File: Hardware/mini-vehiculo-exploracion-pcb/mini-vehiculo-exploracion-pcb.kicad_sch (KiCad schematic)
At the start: 23 parts, among them IC1 BME690, J1 ArducamMINIOV2640, J3 Drivers_Conn_1x8, J4 Drivers_Conn_1x4, J5 Aux_Conn_1x4, J6 RC_Conn_1x4, U1 BNO086, U2 ESP32-S3-WROOM-1, Y1 830003000

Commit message: Add battery sensor
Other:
- sheet MCU renamed MCU_Peripherals
- added sheet Battery_sensor (battery_sensor.kicad_sch)
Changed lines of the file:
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@@
 	)
 	(sheet
-		(at 234.95 90.17)
-		(size 40.64 24.13)
+		(at 234.315 138.43)
+		(size 33.02 17.145)
 		(exclude_from_sim no)
 		(in_bom yes)
@@
 			(color 0 0 0 0.0000)
 		)
-		(property "Sheetname" "MCU"
+		(property "Sheetname" "Battery_sensor"
+			(at 234.315 137.7184 0)
+			(effects
+				(font
+					(size 1.27 1.27)
+				)
+				(justify left bottom)
+			)
+		)
+		(property "Sheetfile" "battery_sensor.kicad_sch"
+			(at 234.315 156.1596 0)
+			(effects
+				(font
+					(size 1.27 1.27)
+				)
+				(justify left top)
+			)
+		)
+		(instances
+			(project "mini-vehiculo-exploracion-pcb"
+				(path "/3cb3b833-c38f-47b4-b7e9-f0e6337b7613"
+					(page "4")
+				)
+			)
+		)
+	)
+	(sheet
+		(at 234.95 90.17)
+		(size 32.385 17.145)
+		(exclude_from_sim no)
+		(in_bom yes)
+		(on_board yes)
+		(dnp no)
+		(fields_autoplaced yes)
+		(stroke
+			(width 0.1524)
+			(type solid)
+		)
+		(fill
+			(color 0 0 0 0.0000)
+		)
+		(property "Sheetname" "MCU_Peripherals"
 			(at 234.95 89.4584 0)
 			(effects
@@
 		)
 		(property "Sheetfile" "mcu.kicad_sch"
-			(at 234.95 114.8846 0)
+			(at 234.95 107.8996 0)
 			(effects
 				(font
@@
 	)
 	(sheet
-		(at 234.95 124.46)
+		(at 234.315 114.3)
 		(size 33.02 16.51)
 		(exclude_from_sim no)
@@
 		)
 		(property "Sheetname" "Electrical"
-			(at 234.95 123.7484 0)
+			(at 234.315 113.5884 0)
 			(effects
 				(font
@@
 		)
 		(property "Sheetfile" "electrical.kicad_sch"
-			(at 234.95 141.5546 0)
+			(at 234.315 131.3946 0)
 			(effects
 				(font

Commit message: changes
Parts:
- C1: footprint (none) -> Capacitor_SMD:C_0805_2012Metric_Pad1.18x1.45mm_HandSolder
- IC1: footprint BME690 -> BME690:BME690
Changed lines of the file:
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@@
 			)
 		)
-		(property "Footprint" "BME690"
+		(property "Footprint" "BME690:BME690"
 			(at 139.7 204.14 0)
 			(effects
@@
 			)
 		)
-		(property "Footprint" ""
+		(property "Footprint" "Capacitor_SMD:C_0805_2012Metric_Pad1.18x1.45mm_HandSolder"
 			(at 35.2552 44.45 0)
 			(effects

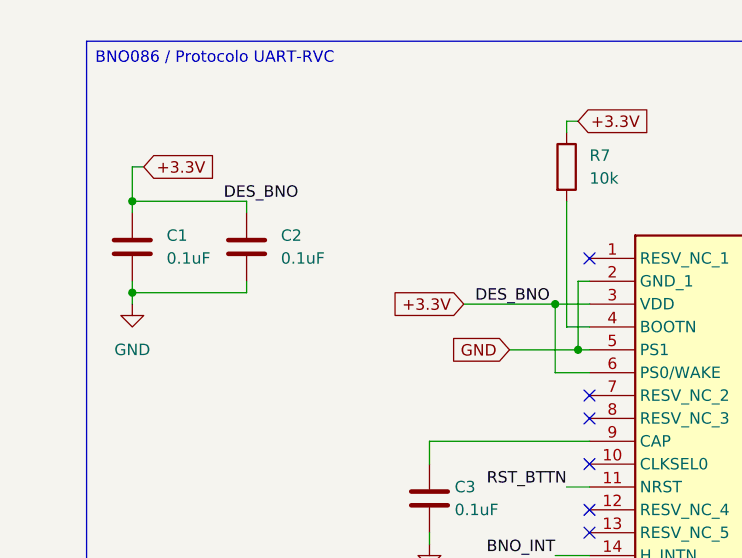
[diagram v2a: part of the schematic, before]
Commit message: Add footprints
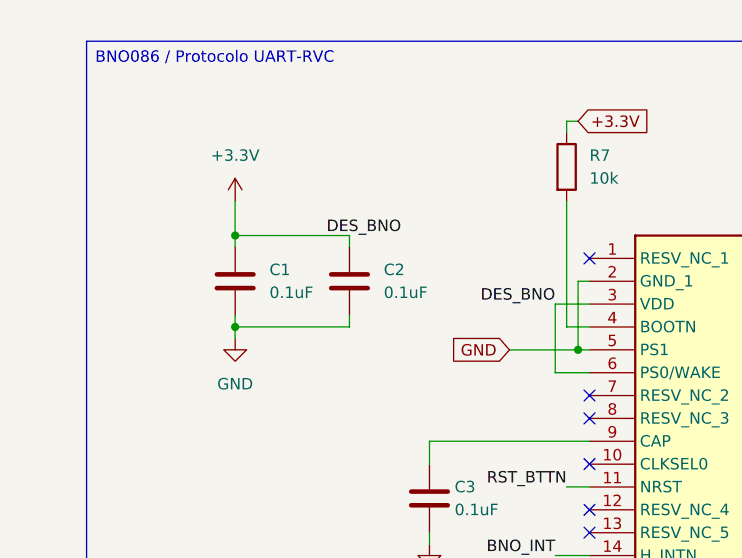
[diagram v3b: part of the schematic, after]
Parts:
- C2, C3, C4, C5, C6, C7: footprint (none) -> Capacitor_SMD:C_0805_2012Metric_Pad1.18x1.45mm_HandSolder
- J3: footprint (none) -> Connector_PinSocket_2.54mm:PinSocket_1x08_P2.54mm_Vertical
- J4, J5, J6: footprint (none) -> Connector_PinSocket_2.54mm:PinSocket_1x04_P2.54mm_Vertical
- R1, R2, R5, R6, R7, R8, R9: footprint (none) -> Resistor_SMD:R_0805_2012Metric_Pad1.20x1.40mm_HandSolder
- U1: footprint BNO086 -> BNO086:BNO086
- Y1: footprint 830003000 -> 830003000:830003000
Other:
- moved on the sheet: C1, C2

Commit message: innit pcb
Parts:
- added J7: Battery_Terminal_01x02, TerminalBlock:TerminalBlock_Xinya_XY308-2.54-2P_1x02_P2.54mm_Horizontal, symbol Connector:Screw_Terminal_01x02
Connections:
- net GND: now also J7.2 (Pin_2)
- new net ENT_BAT: J7.1 (Pin_1)
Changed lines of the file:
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@@
 	(wire
 		(pts
+			(xy 140.97 160.02) (xy 149.86 160.02)
+		)
+		(stroke
+			(width 0)
+			(type default)
+		)
+	)
+	(wire
+		(pts
 			(xy 81.28 74.93) (xy 85.09 74.93)
 		)
@@
 	(wire
 		(pts
+			(xy 144.78 157.48) (xy 149.86 157.48)
+		)
+		(stroke
+			(width 0)
+			(type default)
+		)
+	)
+	(wire
+		(pts
 			(xy 146.05 109.22) (xy 146.05 96.52)
 		)
@@
 		)
 	)
+	(global_label "ENT_BAT"
+		(shape input)
+		(at 144.78 157.48 180)
+		(fields_autoplaced yes)
+		(effects
+			(font
+				(size 1.27 1.27)
+			)
+			(justify right)
+		)
+		(property "Intersheetrefs" "${INTERSHEET_REFS}"
+			(at 134.0539 157.48 0)
+			(effects
+				(font
+					(size 1.27 1.27)
+				)
+				(justify right)
+				(hide yes)
+			)
+		)
+	)
 	(global_label "+3.3V"
 		(shape input)
@@
 	(global_label "GND"
 		(shape input)
+		(at 140.97 160.02 180)
+		(fields_autoplaced yes)
+		(effects
+			(font
+				(size 1.27 1.27)
+			)
+			(justify right)
+		)
+		(property "Intersheetrefs" "${INTERSHEET_REFS}"
+			(at 134.1143 160.02 0)
+			(effects
+				(font
+					(size 1.27 1.27)
+				)
+				(justify right)
+				(hide yes)
+			)
+		)
+	)
+	(global_label "GND"
+		(shape input)
 		(at 137.16 67.31 0)
 		(fields_autoplaced yes)
@@
 					(unit 1)
 				)
+			)
+		)
+	)
+	(symbol
+		(lib_id "Connector:Screw_Terminal_01x02")
+		(at 154.94 157.48 0)
+		(unit 1)
+		(exclude_from_sim no)
+		(in_bom yes)
+		(on_board yes)
+		(dnp no)
+		(fields_autoplaced yes)
+		(property "Reference" "J7"
+			(at 157.48 157.4799 0)
+			(effects
+				(font
+					(size 1.27 1.27)
+				)
+				(justify left)
+			)
+		)
+		(property "Value" "Battery_Terminal_01x02"
+			(at 157.48 160.0199 0)
+			(effects
+				(font
+					(size 1.27 1.27)
+				)
+				(justify left)
+			)
+		)
+		(property "Footprint" "TerminalBlock:TerminalBlock_Xinya_XY308-2.54-2P_1x02_P2.54mm_Horizontal"
+			(at 154.94 157.48 0)
+			(effects
+				(font
+					(size 1.27 1.27)
+				)
+				(hide yes)
+			)
+		)
+		(property "Datasheet" "~"
+			(at 154.94 157.48 0)
+			(effects
+				(font
+					(size 1.27 1.27)
+				)
+				(hide yes)
+			)
+		)
+		(property "Description" "Generic screw terminal, single row, 01x02, script generated (kicad-library-utils/schlib/autogen/connector/)"
+			(at 154.94 157.48 0)
+			(effects
+				(font
+					(size 1.27 1.27)
+				)
+				(hide yes)
+			)
+		)
+		(pin "1"
+		)
+		(pin "2"
+		)
+		(instances
+			(project ""
+				(path "/3cb3b833-c38f-47b4-b7e9-f0e6337b7613"
+					(reference "J7")
+					(unit 1)
+				)

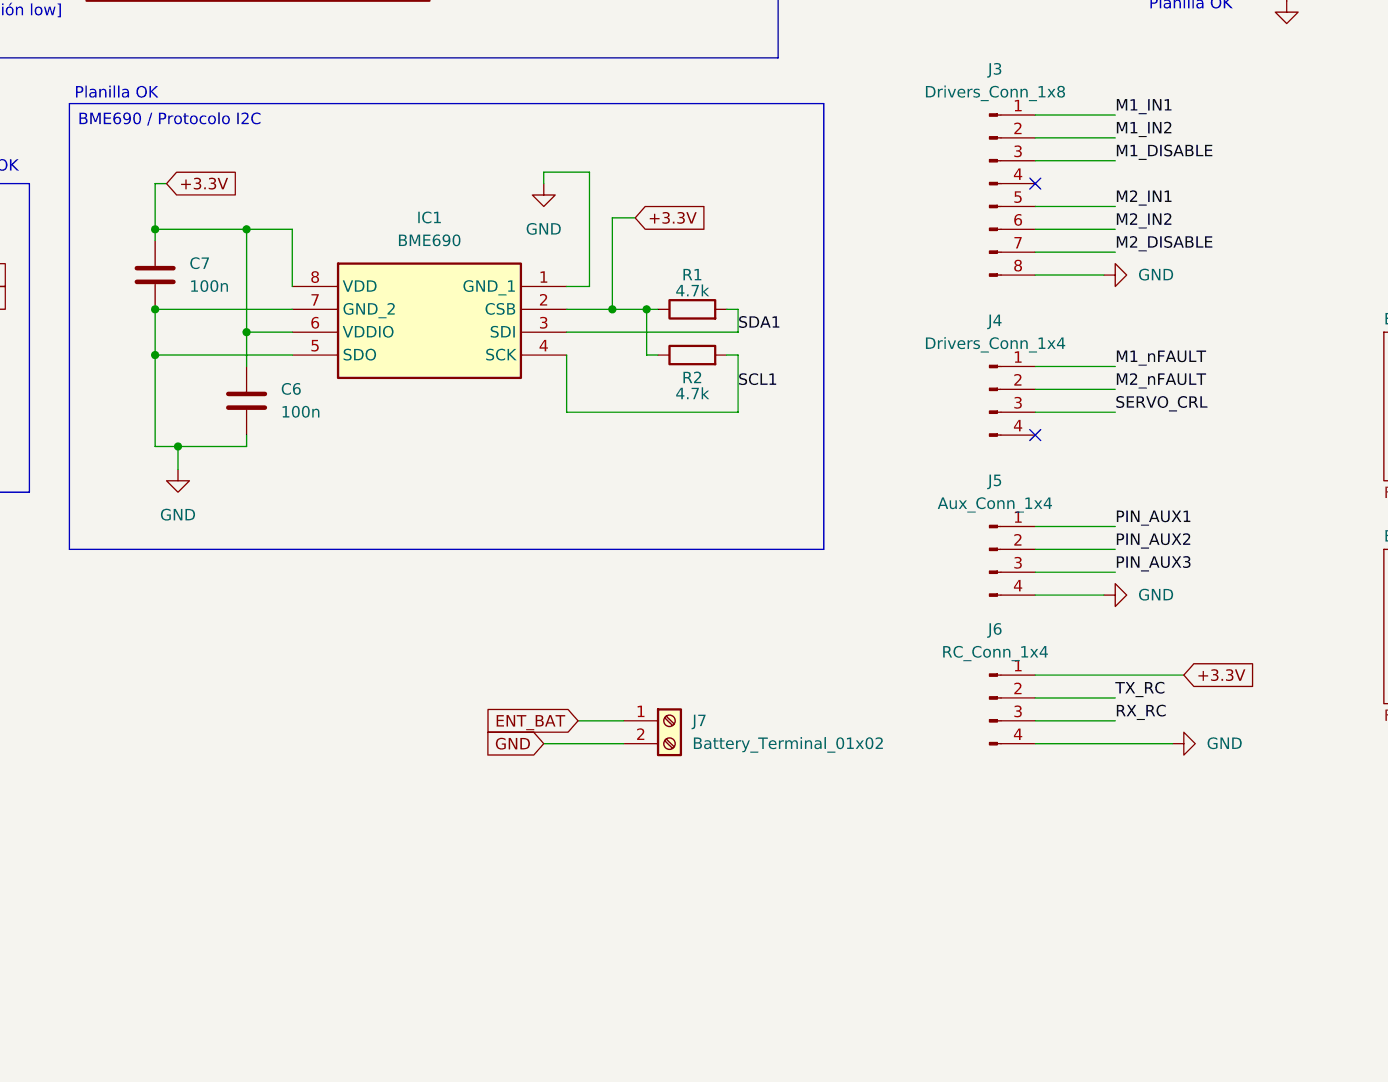
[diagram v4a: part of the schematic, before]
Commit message: Revert "fix bug pcb"
This reverts commit 95896929b2c40d1d86d6f174368d0f9d923b36b5.
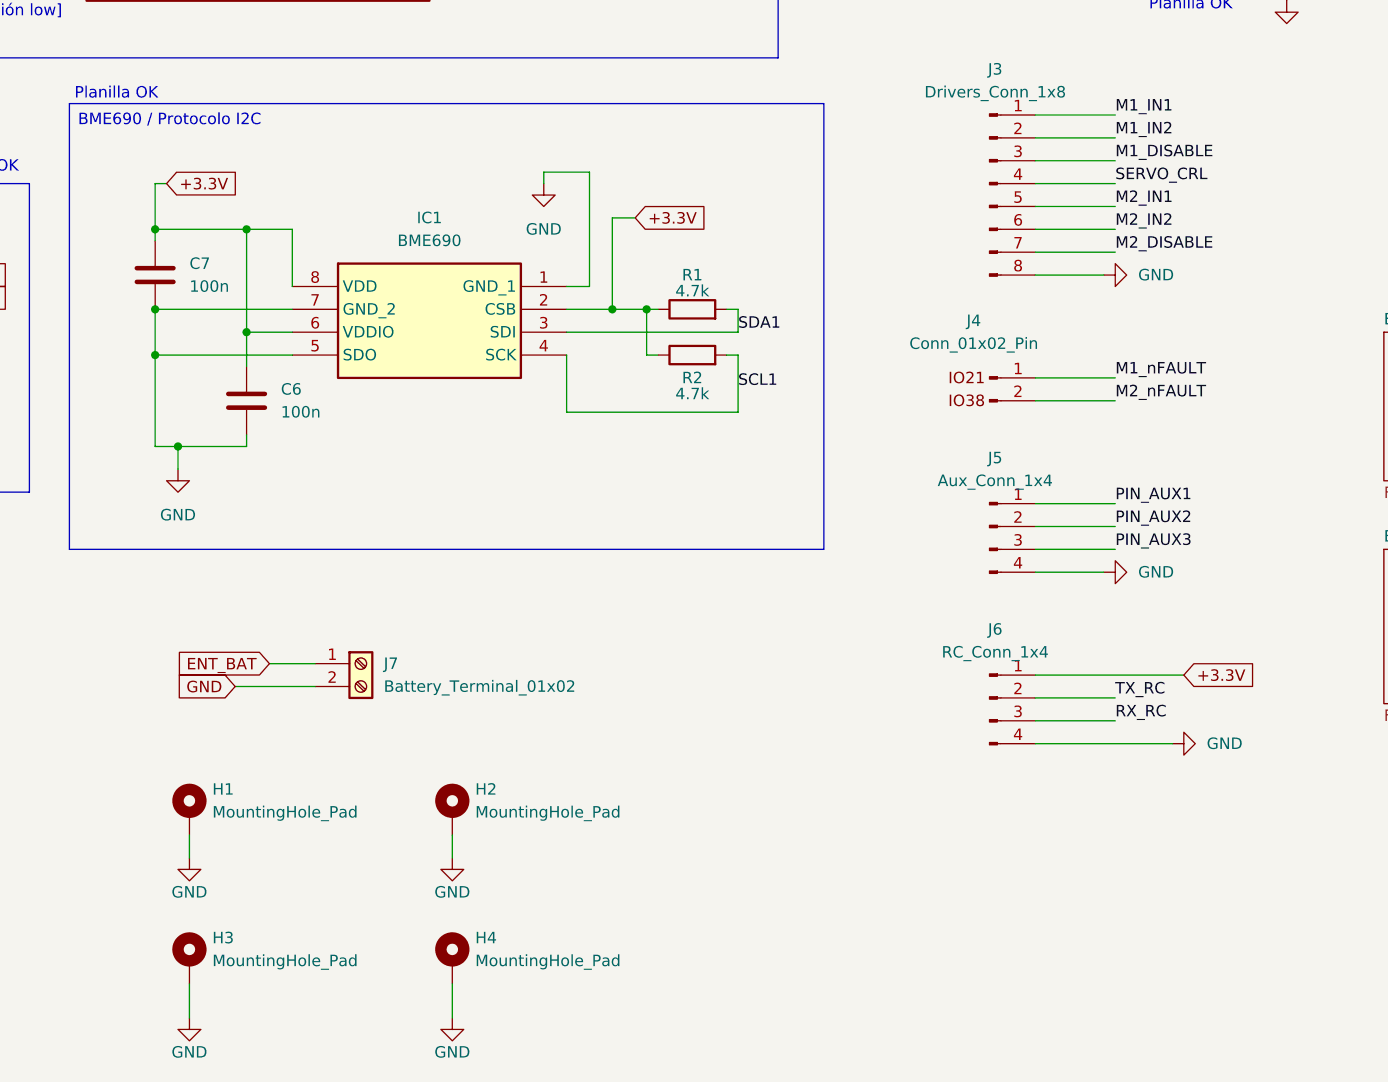
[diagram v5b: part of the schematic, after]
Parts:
- removed J4: Drivers_Conn_1x4, Connector_PinSocket_2.54mm:PinSocket_1x04_P2.54mm_Vertical, symbol Connector:Conn_01x04_Pin
- added H1, H2, H3, H4: MountingHole_Pad, MountingHole:MountingHole_3.2mm_M3_Pad_Via, symbol Mechanical:MountingHole_Pad
- added J4: Conn_01x02_Pin, Connector_PinSocket_2.54mm:PinSocket_1x02_P2.54mm_Vertical, symbol ConectorDriverESP:Conn_01x02_Pin
- J7: footprint TerminalBlock:TerminalBlock_Xinya_XY308-2.54-2P_1x02_P2.54mm_Horizontal -> TerminalBlock_Phoenix:TerminalBlock_Phoenix_MPT-0,5-2-2.54_1x02_P2.54mm_Horizontal
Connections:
- net GND: now also H1.1, H2.1, H3.1, H4.1
- net M1_nFAULT: now also J4.1 (Pin_1)
- net M2_nFAULT: now also J4.2 (Pin_2)
- net SERVO_CRL: now also J3.4 (Pin_4)
- no-connect marks 20 -> 18
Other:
- moved on the sheet: J5, J7

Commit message: continue pcb
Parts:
- added C23, C24: 0.1uF, Capacitor_SMD:C_0805_2012Metric_Pad1.18x1.45mm_HandSolder, symbol Device:C
- added IC2: TXU0104PWR, TXU0104PWR:SOP65P640X120-14N, symbol TXU0104PWR:TXU0104PWR
- added J8: Conn_01x03_Pin, Connector_PinSocket_2.54mm:PinSocket_1x03_P2.54mm_Vertical, symbol Connector:Conn_01x03_Pin
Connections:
- net +3.3V: now also C23.1, IC2.1 (VCCA)
- net GND: now also C23.2, C24.2, IC2.7 (GND), IC2.8 (OE), J8.1 (Pin_1)
- net SERVO_CRL: now also IC2.2 (A1); no longer J3.4 (Pin_4)
- new net SERVO_SAL: IC2.13 (B1Y), J8.3 (Pin_3)
- new net V_SELEC: C24.1, IC2.14 (VCCB), J8.2 (Pin_2)
- no-connect marks 18 -> 27
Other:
- moved on the sheet: H1, H2, H3, H4, J1, J7
